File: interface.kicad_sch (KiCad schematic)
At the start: 0 parts

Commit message: wen branch and pr
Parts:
- added C68, C69, C81, C82, C83, C85, C87, C89, C91, C92, C93, C95, C96, C97, C98: 100n, 0_resistor_smd:R_0603_1608Metric, symbol Device:C
- added C84, C86, C88, C90, C94: 22u, symbol Device:C_Polarized
- added J10, J11, J14, J6, J9: XH2.5-3P, symbol 0_connectors:Conn_01x03_Mounting
- added J12, J13, J15, J3, J5: GH1.25-4P, symbol 0_connectors:Conn_01x04_Mounting
- added J16, J17: GH1.25-2P, symbol 0_connectors:Conn_01x02_Mounting
- added J18: GH1.25-5P, symbol 0_connectors:Conn_01x05_Mounting
- added J7: GH1.25-8P, symbol 0_connectors:Conn_01x08_Mounting
- added J8: GH1.25-6P, symbol 0_connectors:Conn_01x06_Mounting
- added JP3, JP4: J, symbol 0_misc:SolderJumper_2_Bridged
- added R37, R38, R39, R40, R58, R59: 22R, 0_resistor_smd:R_0402_1005Metric, symbol Device:R
- added R52, R53: 120R, 0_resistor_smd:R_0402_1005Metric, symbol Device:R
- added R54, R55, R56, R57, R60: 47k, symbol Device:R
- added R61: 68k, symbol Device:R
- added R62: 10k, symbol Device:R
- added U15: LPW5209AB5F, symbol 0_power:LPW5209AB5F
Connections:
- new net: J15.2 (Pin_2), R58.1
- new net: R60.1, U15.3 (RSET)
- new net: J12.3 (Pin_2), R52.1
- new net: JP3.1 (A), R52.2
- new net: J13.3 (Pin_2), R53.1
- new net: JP4.1 (A), R53.2
- new net: J16.1 (Pin_1), R61.1
- new net: C97.1, J17.1 (Pin_1), U15.1 (VOUT)
- new net: J13.2 (Pin_2), JP4.2 (B)
- new net: J3.3 (Pin_2), R37.1
- new net: J5.3 (Pin_2), R40.1
- new net: J5.2 (Pin_2), R39.1
- new net: J3.2 (Pin_2), R38.1
- new net: J15.3 (Pin_2), R59.1
- new net: J12.2 (Pin_2), JP3.2 (B)
- new net +5V: C68.1, C69.1, C81.1, C82.1, C91.1, C92.1, C95.1, C98.1, J12.1 (Pin_1), J13.1 (Pin_1), J15.1 (Pin_1), J18.1 (Pin_1), J3.1 (Pin_1), J5.1 (Pin_1), J7.1 (Pin_1), J8.1 (Pin_1), U15.5 (VIN)
- new net +5V_EXT: C93.1, C94.1, J14.1 (Pin_1)
- new net +BAT: C83.1, C84.1, C85.1, C86.1, C87.1, C88.1, C89.1, C90.1, J10.1 (Pin_1), J11.1 (Pin_1), J6.1 (Pin_1), J9.1 (Pin_1)
- new net CAM_EN: U15.4 (EN)
- new net EXT_BAT_VMON: C96.1, R61.2, R62.1
- new net EXT_LED_DATA: J14.2 (Pin_2)
- new net GND: C68.2, C69.2, C81.2, C82.2, C83.2, C84.2, C85.2, C86.2, C87.2, C88.2, C89.2, C90.2, C91.2, C92.2, C93.2, C94.2, C95.2, C96.2, C97.2, C98.2, J10.3 (Pin_2), J10.MP1, J10.MP2, J11.3 (Pin_2), J11.MP1, J11.MP2, J12.4 (Pin_2), J12.MP1, J12.MP2, J13.4 (Pin_2), J13.MP1, J13.MP2, J14.3 (Pin_2), J14.MP1, J14.MP2, J15.4 (Pin_2), J15.MP1, J15.MP2, J16.2 (Pin_2), J16.MP1, J16.MP2, J17.2 (Pin_2), J17.MP1, J17.MP2, J18.5 (Pin_5), J18.MP1, J18.MP2, J3.4 (Pin_2), J3.MP1, J3.MP2, J5.4 (Pin_2), J5.MP1, J5.MP2, J6.3 (Pin_2), J6.MP1, J6.MP2, J7.8 (Pin_8), J7.MP1, J7.MP2, J8.6 (Pin_6), J8.MP1, J8.MP2, J9.3 (Pin_2), J9.MP1, J9.MP2, R54.2, R55.2, R56.2, R57.2, R60.2, R62.2, U15.2 (GND)
- new net NRST: J18.4 (Pin_4)
- new net PWM1: J6.2 (Pin_2), R56.1
- new net PWM2: J9.2 (Pin_2), R55.1
- new net PWM3: J10.2 (Pin_2), R54.1
- new net PWM4: J11.2 (Pin_2), R57.1
- new net RTK_EVT: J8.5 (Pin_5)
- new net RTK_PPS: J8.4 (Pin_4)
- new net SWCLK: J18.3 (Pin_3)
- new net SWDIO: J18.2 (Pin_2)
- new net VN_PPS: J7.4 (Pin_4)
- new net VN_SYNC: J7.5 (Pin_5)
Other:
- note added: "5V OUTPUT @ 1000 mA"
- note added: "BATTERY VMON INPUT"
- note added: "ESC #1"
- note added: "ESC #2"
- note added: "FDCAN #1"
- note added: "FDCAN #2"
- note added: "LED STRIP"
- note added: "LIDAR INTERFACE #1"
- note added: "LIDAR INTERFACE #2"
- note added: "SERIAL WIRE DEBUG"
- note added: "SERVO #1"
- note added: "SERVO #2"
- note added: "UART RADIO"
- note added: "VN300 INTEREFACE"
- note added: "ZED X20P INTERFACE"
- title: (none) -> Interfaces

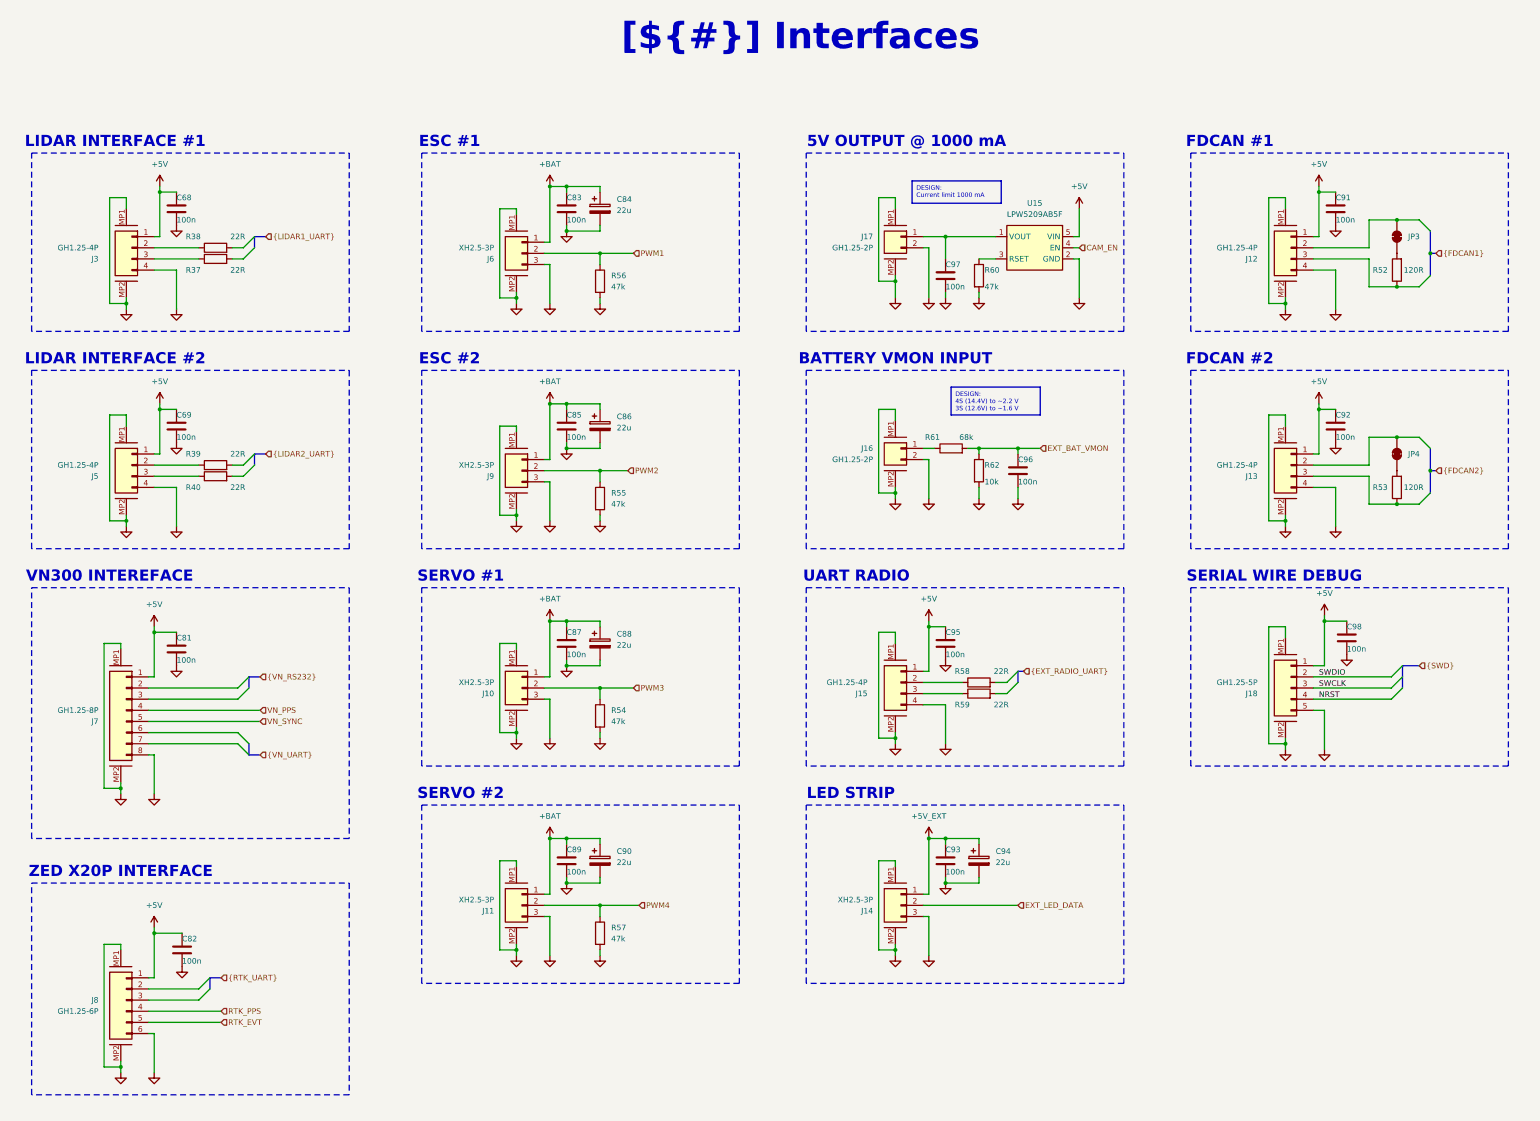
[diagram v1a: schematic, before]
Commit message: much work and .ioc file added
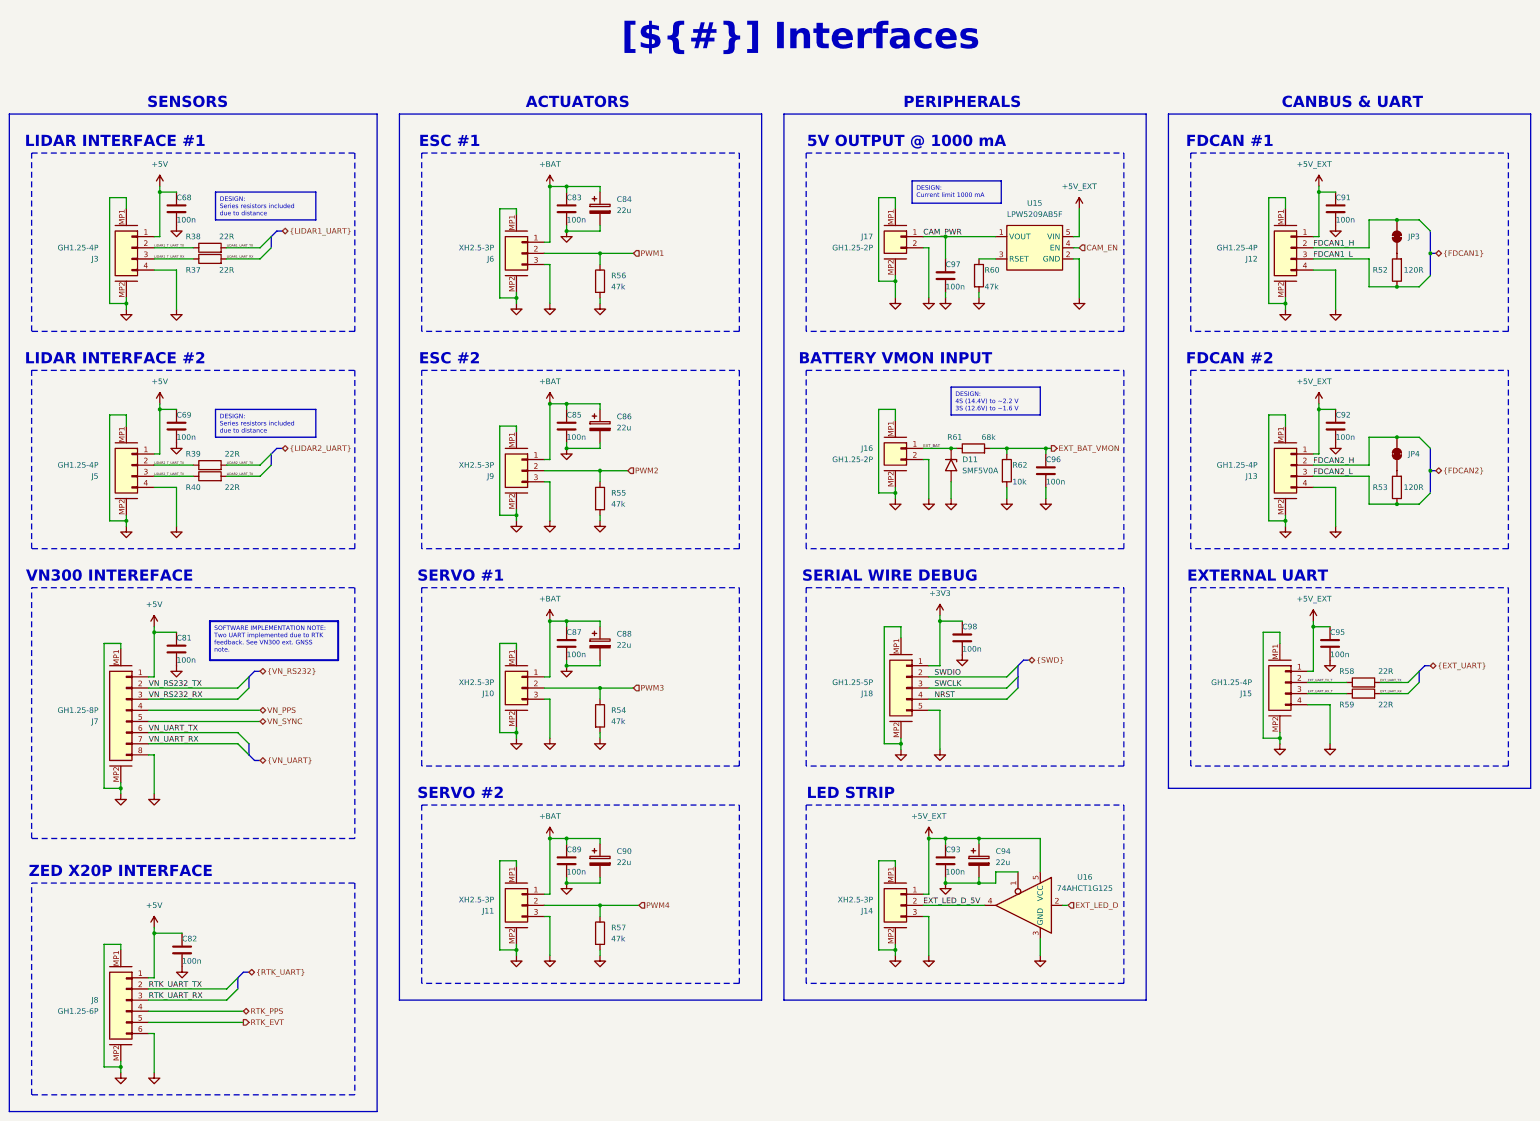
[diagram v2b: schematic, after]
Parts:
- added D11: SMF5V0A, Diode_SMD:D_SMF, symbol 0_diodes:SMF5V0A
- added U16: 74AHCT1G125, symbol 0_transceivers:74AHCT1G125
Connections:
- net +5V: no longer C91.1, C92.1, C95.1, C98.1, J12.1 (Pin_1), J13.1 (Pin_1), J15.1 (Pin_1), J18.1 (Pin_1), U15.5 (VIN)
- net +5V_EXT: now also C91.1, C92.1, C95.1, J12.1 (Pin_1), J13.1 (Pin_1), J15.1 (Pin_1), U15.5 (VIN), U16.5 (VCC)
- net GND: now also D11.2 (A2), U16.1, U16.3 (GND)
- net EXT_UART_TX_T: now reaches J15.2 (Pin_2), R58.1
- net EXT_UART_TX: now reaches R58.2
- net RTK_UART_TX: now reaches J8.2 (Pin_2)
- net RTK_UART_RX: now reaches J8.3 (Pin_3)
- net FDCAN1_L: now reaches J12.3 (Pin_2), R52.1
- net FDCAN2_L: now reaches J13.3 (Pin_2), R53.1
- net EXT_BAT: now reaches J16.1 (Pin_1), R61.1
- net EXT_BAT: now also D11.1 (A1)
- net CAM_PWR: now reaches C97.1, J17.1 (Pin_1), U15.1 (VOUT)
- net FDCAN2_H: now reaches J13.2 (Pin_2), JP4.2 (B)
- net LIDAR1_T_UART_RX: now reaches J3.3 (Pin_2), R37.1
- net LIDAR1_UART_RX: now reaches R37.2
- net LIDAR2_T_UART_TX: now reaches J5.3 (Pin_2), R40.1
- net LIDAR2_T_UART_TX: now also J5.2 (Pin_2), R39.1
- net LIDAR2_UART_TX: now reaches R40.2
- net LIDAR2_UART_TX: now also R39.2
- net LIDAR1_T_UART_TX: now reaches J3.2 (Pin_2), R38.1
- net EXT_UART_RX_T: now reaches J15.3 (Pin_2), R59.1
- net LIDAR1_UART_TX: now reaches R38.2
- net FDCAN1_H: now reaches J12.2 (Pin_2), JP3.2 (B)
- net EXT_UART_RX: now reaches R59.2
- net VN_RS232_TX: now reaches J7.2 (Pin_2)
- net VN_RS232_RX: now reaches J7.3 (Pin_3)
- net VN_UART_TX: now reaches J7.6 (Pin_6)
- net VN_UART_RX: now reaches J7.7 (Pin_7)
- net EXT_LED_DATA renamed EXT_LED_D_5V
- net EXT_LED_D_5V: now also U16.4
- new net +3V3: C98.1, J18.1 (Pin_1)
- new net EXT_LED_D: U16.2
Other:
- note added: "ACTUATORS"
- note added: "CANBUS & UART"
- note added: "EXTERNAL UART"
- note added: "PERIPHERALS"
- note added: "SENSORS"
- note removed: "UART RADIO"
- moved on the sheet: C95, C96, C98, J15, J18, R37, R38, R39, R40, R58, R59, R61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

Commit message: start fix fp
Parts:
- added JP5: SolderJumper_3_Open, Jumper:SolderJumper-3_P1.3mm_Open_Pad1.0x1.5mm, symbol Jumper:SolderJumper_3_Open
- D11: footprint Diode_SMD:D_SMF -> 0_diodes:D_SMF
- U16: footprint (none) -> Package_TO_SOT_SMD:SOT-353_SC-70-5
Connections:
- net +3V3: now also JP5.3 (B)
- net +5V: now also JP5.1 (A)
- net +5V_EXT: no longer C95.1, J15.1 (Pin_1)
- new net: C95.1, J15.1 (Pin_1), JP5.2 (C)
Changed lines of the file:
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@@
 	)
 	(junction
+		(at 334.01 158.75)
+		(diameter 0)
+		(color 0 0 0 0)
+	)
+	(junction
 		(at 247.65 118.11)
 		(diameter 0)
@@
 	)
 	(junction
-		(at 330.2 158.75)
-		(diameter 0)
-		(color 0 0 0 0)
-	)
-	(junction
 		(at 59.69 85.09)
 		(diameter 0)
@@
 		)
 	)
+	(wire
+		(pts
+			(xy 353.06 154.94) (xy 356.87 154.94)
+		)
+		(stroke
+			(width 0)
+			(type default)
+		)
+	)
 	(bus
 		(pts
@@
 	(wire
 		(pts
+			(xy 334.01 158.75) (xy 347.98 158.75)
+		)
+		(stroke
+			(width 0)
+			(type default)
+		)
+	)
+	(wire
+		(pts
 			(xy 160.02 58.42) (xy 167.64 58.42)
 		)
@@
 	(wire
 		(pts
+			(xy 339.09 154.94) (xy 342.9 154.94)
+		)
+		(stroke
+			(width 0)
+			(type default)
+		)
+	)
+	(wire
+		(pts
 			(xy 323.85 60.96) (xy 323.85 63.5)
 		)
@@
 		)
 	)
-	(wire
-		(pts
-			(xy 330.2 157.48) (xy 330.2 158.75)
-		)
-		(stroke
-			(width 0)
-			(type default)
-		)
-	)
 	(bus
 		(pts
@@
 			)
 		)
-		(property "Footprint" ""
+		(property "Footprint" "Package_TO_SOT_SMD:SOT-353_SC-70-5"
 			(at 262.89 222.25 0)
 			(effects
@@
 	)
 	(symbol
+		(lib_id "Jumper:SolderJumper_3_Open")
+		(at 347.98 154.94 0)
+		(unit 1)
+		(exclude_from_sim no)
+		(in_bom no)
+		(on_board yes)
+		(dnp no)
+		(property "Reference" "JP5"
+			(at 347.98 152.4 0)
+			(effects
+				(font
+					(size 1.27 1.27)
+				)
+			)
+		)
+		(property "Value" "SolderJumper_3_Open"
+			(at 347.98 151.13 0)
+			(effects
+				(font
+					(size 1.27 1.27)
+				)
+				(hide yes)
+			)
+		)
+		(property "Footprint" "Jumper:SolderJumper-3_P1.3mm_Open_Pad1.0x1.5mm"
+			(at 347.98 154.94 0)
+			(effects
+				(font
+					(size 1.27 1.27)
+				)
+				(hide yes)
+			)
+		)
+		(property "Datasheet" "~"
+			(at 347.98 154.94 0)
+			(effects
+				(font
+					(size 1.27 1.27)
+				)
+				(hide yes)
+			)
+		)
+		(property "Description" "Solder Jumper, 3-pole, open"
+			(at 347.98 154.94 0)
+			(effects
+				(font
+					(size 1.27 1.27)
+				)
+				(hide yes)
+			)
+		)
+		(pin "2"
+		)
+		(pin "1"
+		)
+		(pin "3"
+		)
+		(instances
+			(project ""
+				(path "/abe950a1-9eef-4508-9fd4-31d3e723e029/c85454e5-a89e-41eb-a5ed-71b4fc4cf13a/1b965b44-1377-4308-8bb4-a6ed39c8528f"
+					(reference "JP5")
+					(unit 1)
+				)
+			)
+		)
+	)
+	(symbol
 		(lib_id "power:GND")
 		(at 245.11 186.69 0)
@@
 	)
 	(symbol
-		(lib_id "power:+3.3V")
-		(at 330.2 157.48 0)
-		(unit 1)
-		(exclude_from_sim no)
-		(in_bom yes)
-		(on_board yes)
-		(dnp no)
-		(property "Reference" "#PWR0182"
-			(at 330.2 161.29 0)
-			(effects
-				(font
-					(size 1.27 1.27)
-				)
-				(hide yes)
-			)
-		)
-		(property "Value" "+5V_EXT"
-			(at 326.39 152.4 0)
-			(effects
-				(font
-					(size 1.27 1.27)
-				)
-				(justify left)
-			)
-		)
-		(property "Footprint" ""
-			(at 330.2 157.48 0)
-			(effects
-				(font
-					(size 1.27 1.27)
-				)
-				(hide yes)
-			)
-		)
-		(property "Datasheet" ""
-			(at 330.2 157.48 0)
-			(effects
-				(font
-					(size 1.27 1.27)
-				)
-				(hide yes)
-			)
-		)
-		(property "Description" "Power symbol creates a global label with name \"+3.3V\""
-			(at 330.2 157.48 0)
-			(effects
-				(font
-					(size 1.27 1.27)
-				)
-				(hide yes)
-			)
-		)
-		(pin "1"
-		)
-		(instances
-			(project "hoppen_fc"
-				(path "/abe950a1-9eef-4508-9fd4-31d3e723e029/c85454e5-a89e-41eb-a5ed-71b4fc4cf13a/1b965b44-1377-4308-8bb4-a6ed39c8528f"
-					(reference "#PWR0182")
-					(unit 1)
-				)
-			)
-		)
-	)
-	(symbol
 		(lib_id "power:GND")
 		(at 234.95 233.68 0)
@@
 			)
 		)
-		(property "Footprint" "Diode_SMD:D_SMF"
+		(property "Footprint" "0_diodes:D_SMF"
 			(at 261.62 121.92 0)
 			(effects
@@
 	(symbol
 		(lib_id "power:+3.3V")
+		(at 339.09 154.94 0)
+		(unit 1)
+		(exclude_from_sim no)
+		(in_bom yes)
+		(on_board yes)
+		(dnp no)
+		(property "Reference" "#PWR0103"
+			(at 339.09 158.75 0)
+			(effects
+				(font
+					(size 1.27 1.27)
+				)
+				(hide yes)
+			)
+		)
+		(property "Value" "+5V"
+			(at 333.502 153.416 0)
+			(effects
+				(font
+					(size 1.27 1.27)
+				)
+				(justify left)
+			)
+		)
+		(property "Footprint" ""
+			(at 339.09 154.94 0)
+			(effects
+				(font
+					(size 1.27 1.27)
+				)
+				(hide yes)
+			)
+		)
+		(property "Datasheet" ""
+			(at 339.09 154.94 0)
+			(effects
+				(font
+					(size 1.27 1.27)
+				)
+				(hide yes)
+			)
+		)
+		(property "Description" "Power symbol creates a global label with name \"+3.3V\""
+			(at 339.09 154.94 0)
+			(effects
+				(font
+					(size 1.27 1.27)
+				)
+				(hide yes)
+			)
+		)
+		(pin "1"
+		)
+		(instances
+			(project "hoppen_fc"
+				(path "/abe950a1-9eef-4508-9fd4-31d3e723e029/c85454e5-a89e-41eb-a5ed-71b4fc4cf13a/1b965b44-1377-4308-8bb4-a6ed39c8528f"
+					(reference "#PWR0103")
+					(unit 1)
+				)
+			)
+		)
+	)
+	(symbol
+		(lib_id "power:+3.3V")
 		(at 67.31 58.42 0)
 		(unit 1)
@@
 					(unit 1)
 				)
+			)
+		)
+	)
+	(symbol
+		(lib_id "power:+3.3V")
+		(at 356.87 154.94 0)
+		(unit 1)
+		(exclude_from_sim no)
+		(in_bom yes)
+		(on_board yes)
+		(dnp no)
+		(property "Reference" "#PWR0182"
+			(at 356.87 158.75 0)
+			(effects
+				(font
+					(size 1.27 1.27)
+				)
+				(hide yes)
+			)
+		)
+		(property "Value" "+3V3"
+			(at 358.394 153.416 0)
+			(effects
+				(font
+					(size 1.27 1.27)
+				)
+				(justify left)
+			)
+		)
+		(property "Footprint" ""
+			(at 356.87 154.94 0)
+			(effects
+				(font
+					(size 1.27 1.27)
+				)
+				(hide yes)
+			)
+		)
+		(property "Datasheet" ""
+			(at 356.87 154.94 0)
+			(effects
+				(font
+					(size 1.27 1.27)
+				)
+				(hide yes)
+			)
+		)
+		(property "Description" "Power symbol creates a global label with name \"+3.3V\""
+			(at 356.87 154.94 0)
+			(effects
+				(font
+					(size 1.27 1.27)
+				)
+				(hide yes)
+			)
+		)
+		(pin "1"
+		)
+		(instances
+			(project "hoppen_fc"
+				(path "/abe950a1-9eef-4508-9fd4-31d3e723e029/c85454e5-a89e-41eb-a5ed-71b4fc4cf13a/1b965b44-1377-4308-8bb4-a6ed39c8528f"
+					(reference "#PWR0182")
+					(unit 1)
+				)
